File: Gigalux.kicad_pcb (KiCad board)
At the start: 2 copper layers, 101.6 x 17.8 mm, 9 parts, among them P1 IN, P2 OUT, U1 TLC5971

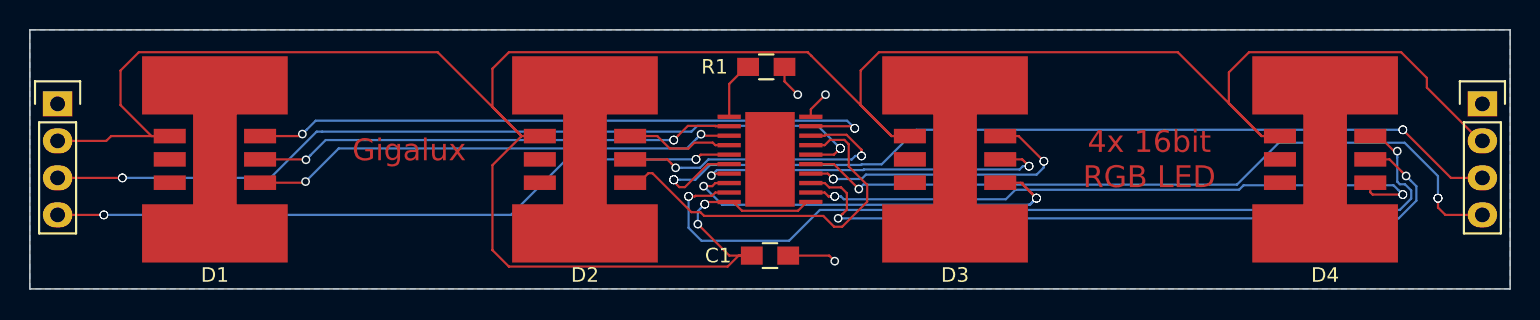
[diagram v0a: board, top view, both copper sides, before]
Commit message: Fixed pinouts for TLC5711, fixed board layout.
This is the one that was sent to OSH park on 7/15
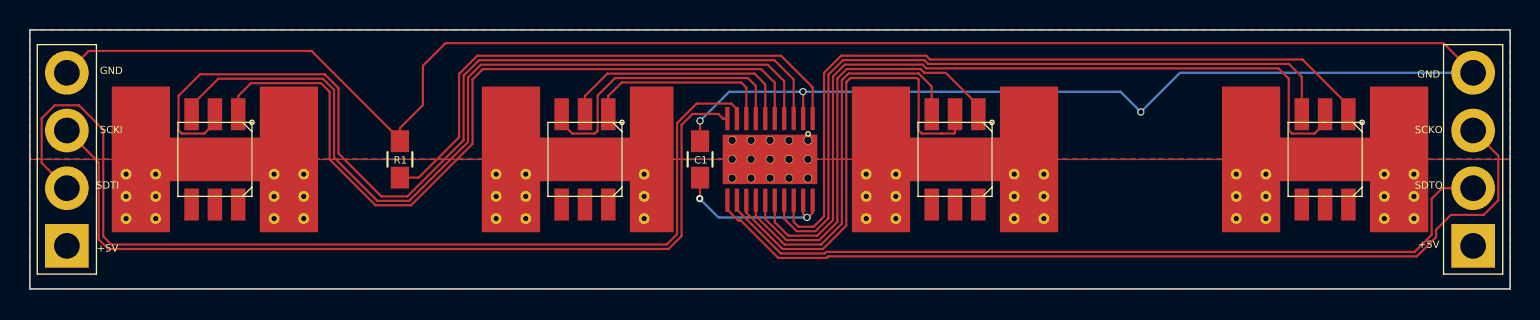
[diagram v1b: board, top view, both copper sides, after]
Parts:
- added REF**: Via, Zetaohm:Via, F.Cu at (171.2, 96.8)
- added REF**: Via, Zetaohm:Via, F.Cu at (159.0, 95.2)
- added REF**: Via, Zetaohm:Via, F.Cu at (161.0, 95.2)
- added REF**: Via, Zetaohm:Via, F.Cu at (161.0, 93.7)
- added REF**: Via, Zetaohm:Via, F.Cu at (145.8, 96.8)
- added REF**: Via, Zetaohm:Via, F.Cu at (143.8, 96.8)
- added REF**: Via, Zetaohm:Via, F.Cu at (143.8, 93.7)
- added REF**: Via, Zetaohm:Via, F.Cu at (143.8, 95.2)
- added REF**: Via, Zetaohm:Via, F.Cu at (145.8, 95.2)
- added REF**: Via, Zetaohm:Via, F.Cu at (145.8, 93.7)
- added REF**: Via, Zetaohm:Via, F.Cu at (135.6, 96.8)
- added REF**: Via, Zetaohm:Via, F.Cu at (169.2, 96.8)
- added REF**: Via, Zetaohm:Via, F.Cu at (133.6, 96.8)
- added REF**: Via, Zetaohm:Via, F.Cu at (133.6, 93.7)
- added REF**: Via, Zetaohm:Via, F.Cu at (133.6, 95.2)
- added REF**: Via, Zetaohm:Via, F.Cu at (135.6, 95.2)
- added REF**: Via, Zetaohm:Via, F.Cu at (135.6, 93.7)
- added REF**: Via, Zetaohm:Via, F.Cu at (118.4, 96.8)
- added REF**: Via, Zetaohm:Via, F.Cu at (118.4, 93.7)
- added REF**: Via, Zetaohm:Via, F.Cu at (118.4, 95.2)
- added REF**: Via, Zetaohm:Via, F.Cu at (110.2, 96.8)
- added REF**: Via, Zetaohm:Via, F.Cu at (108.2, 96.8)
- added REF**: Via, Zetaohm:Via, F.Cu at (169.2, 93.7)
- added REF**: Via, Zetaohm:Via, F.Cu at (108.2, 93.7)
- added REF**: Via, Zetaohm:Via, F.Cu at (108.2, 95.2)
- added REF**: Via, Zetaohm:Via, F.Cu at (110.2, 95.2)
- added REF**: Via, Zetaohm:Via, F.Cu at (110.2, 93.7)
- added REF**: Via, Zetaohm:Via, F.Cu at (95.0, 96.8)
- added REF**: Via, Zetaohm:Via, F.Cu at (93.0, 95.2)
- added REF**: Via, Zetaohm:Via, F.Cu at (95.0, 95.2)
- added REF**: Via, Zetaohm:Via, F.Cu at (95.0, 93.7)
- added REF**: Via, Zetaohm:Via, F.Cu at (93.0, 93.7)
- added REF**: Via, Zetaohm:Via, F.Cu at (93.0, 96.8)
- added REF**: Via, Zetaohm:Via, F.Cu at (169.2, 95.2)
- added REF**: Via, Zetaohm:Via, F.Cu at (84.8, 96.8)
- added REF**: Via, Zetaohm:Via, F.Cu at (82.8, 96.8)
- added REF**: Via, Zetaohm:Via, F.Cu at (82.8, 95.2)
- added REF**: Via, Zetaohm:Via, F.Cu at (84.8, 95.2)
- added REF**: Via, Zetaohm:Via, F.Cu at (84.8, 93.7)
- added REF**: Via, Zetaohm:Via, F.Cu at (82.8, 93.7)
- added REF**: Via, Zetaohm:Via, F.Cu at (171.2, 95.2)
- added REF**: Via, Zetaohm:Via, F.Cu at (171.2, 93.7)
- added REF**: Via, Zetaohm:Via, F.Cu at (161.0, 96.8)
- added REF**: Via, Zetaohm:Via, F.Cu at (159.0, 96.8)
- added REF**: Via, Zetaohm:Via, F.Cu at (159.0, 93.7)
- P1, P2: footprint Pin_Headers:Pin_Header_Straight_1x04 -> Zetaohm:KK396-4Pin
- U1: footprint Zetaohm:TLC59711 -> TLC59711
- moved R1 25.9 mm to (101.6, 92.7), turned to 90 degrees
- moved C1 8.16 mm to (122.2, 92.7), turned to 270 degrees
- moved P2 3.86 mm to (175.3, 92.7)
- moved P1 3.86 mm to (78.7, 92.7)
- turned D1 to 90 degrees
- turned D2 to 90 degrees
- turned D3 to 90 degrees
- turned D4 to 90 degrees
- turned U1 to 270 degrees
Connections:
- P1 pad 2: +5V -> SCKI
- P1 pad 3: SCKI -> SDTI
- P1 pad 4: SDTI -> +5V
- P2 pad 2: +5V -> SCKO
- P2 pad 3: SCKO -> SDTO
- P2 pad 4: SDTO -> +5V
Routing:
- net +5V: track 187.9 -> 12.1 mm, vias 3 -> 2
- net GND: track 7.57 -> 164.3 mm
- net Net-(R1-Pad1): track 4.04 -> 37.4 mm
- net R0: track 33.2 -> 64.5 mm, vias 3 -> 0
- net SDTI: track 47.8 -> 71.1 mm, vias 4 -> 0
- net B0: track 33.6 -> 53.9 mm, vias 2 -> 0
- net G0: track 44.5 -> 57.7 mm, vias 3 -> 0
- net B1: track 26.1 -> 13.4 mm
- net G1: track 7.39 -> 19.7 mm
- net G3: track 62.4 -> 50.8 mm, vias 3 -> 0
- net B3: track 44.4 -> 52.4 mm, vias 4 -> 0
- net R2: track 25.8 -> 32.6 mm, vias 3 -> 0
- net G2: track 20.6 -> 26.9 mm, vias 4 -> 0
- net R3: track 49.8 -> 55.2 mm, vias 2 -> 0
- net SDTO: track 51.4 -> 55.7 mm, vias 4 -> 0
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- added copper zone on B.Cu, net +5V
- added copper zone on F.Cu, net +5V
- added copper zone on F.Cu, net GND
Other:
- net class Default: clearance 0.2 -> 0.153; via_dia 0.6 -> 0.5; via_drill 0.4 -> 0.35
- rule trace_clearance: 0.2 -> 0.153
- board text added: "+5V"
- board text added: "GND"
- board text added: "SCKI"
- board text added: "SCKO"
- board text added: "SDTI"
- board text added: "SDTO"
- board text removed: "4x 16bit RGB LED"
- board text removed: "Gigalux"
